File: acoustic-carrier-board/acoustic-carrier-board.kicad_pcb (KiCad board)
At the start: 6 copper layers, 99 x 97 mm, 445 parts, among them IC1 ECP5-BGA256, IC1101 MT41K256M16TW-107_P, J1001 BWU.FL-IPEX1, J1002 BWU.FL-IPEX1, J1003 BWU.FL-IPEX1, J1004 BWU.FL-IPEX1, J1005 BWU.FL-IPEX1, J1006 BWU.FL-IPEX1, J1007 8P8C_Shielded, J1008 BWU.FL-IPEX1, J1009 BWU.FL-IPEX1, J1010 BWU.FL-IPEX1, J1011 BWU.FL-IPEX1, J1201 HR911130A, J201 Conn_02x06_Odd_Even, J701 Conn_02x03_Odd_Even, J702 PMOD_JTAG, J703 PMOD_SPI, J704 PMOD_GPIO, J801 TYPE-C-31-M-12, J903 Conn_02x06_Odd_Even, Q201 AO3401A, SW602 SW_Push, SW603 SW_Push, SW701 SW_Push, U1001 MS9280, U1002 THS4521IDGK, U1003 DGQ2788AEN-T1-GE4, U1004 LMV321, U1005 TL432DBZ, U1201 KSZ9031RN, U201 TPS2121RUX, U202 TLV62569DBV, U203 TLV62569DBV, U204 TLV62569DBV, U205 TLV62569DBV, U206 OPA376xxDBV, U701 W25Q128JVS, U702 W25Q128JVS, U801 USB3300-EZK, U802 LMV321, Y1201 25MHz, Y401 Crystal Oscillator, Y801 Crystal_GND24_Small

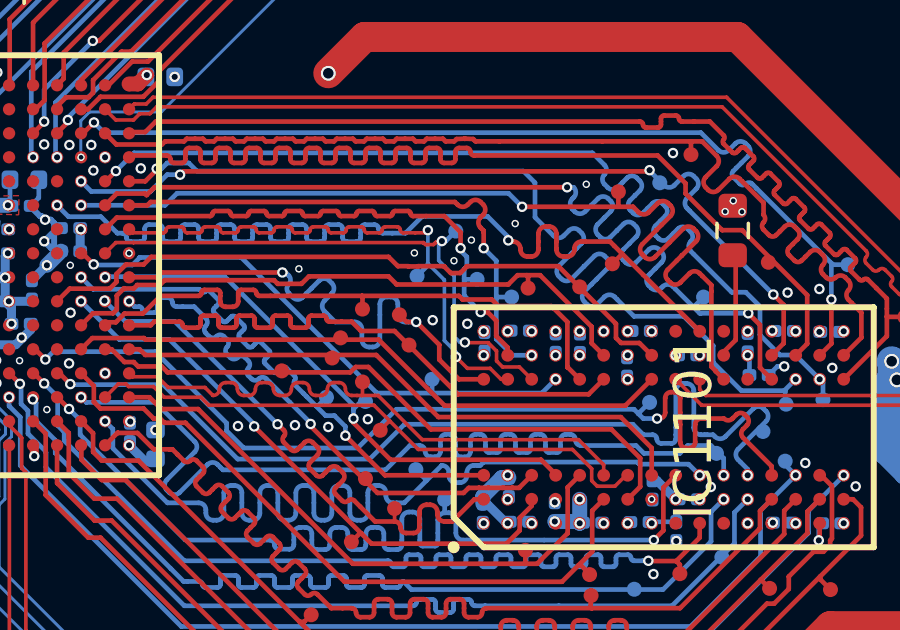
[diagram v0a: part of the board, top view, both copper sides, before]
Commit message: Modified README, lpddr3 testpoint search
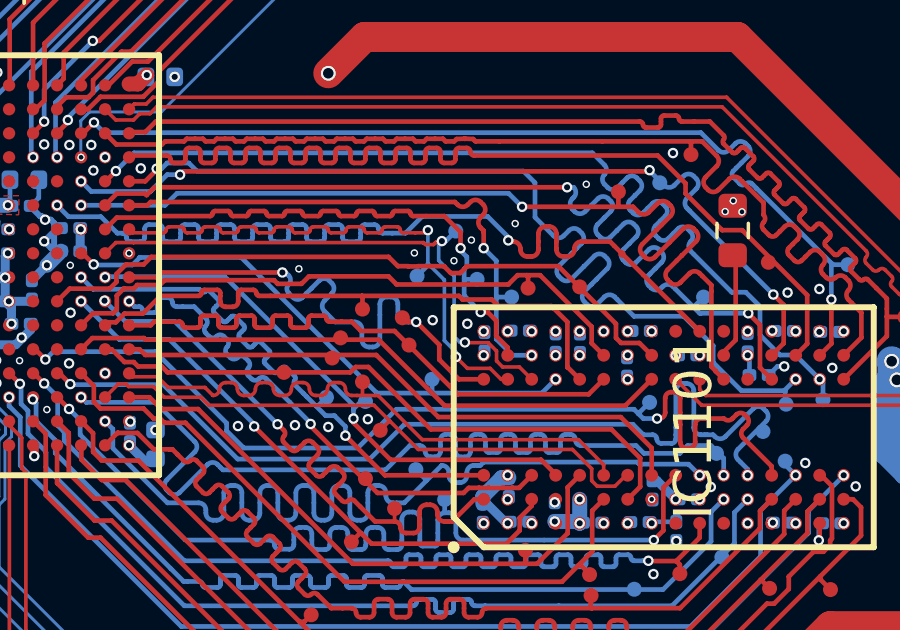
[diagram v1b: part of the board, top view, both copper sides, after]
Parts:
- TP1149: footprint iw-misc:TestPoint_Pad_D0.25mm -> iw-misc:TestPoint_Pad_D0.125mm
- moved TP1149 0.46 mm to (111.3, 87.5)
- moved TP1110 0.14 mm to (104.0, 89.6)
- moved TP1120 0.09 mm to (100.1, 91.4)
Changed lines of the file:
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@@
 	(footprint "iw-misc:TestPoint_Pad_D0.25mm"
 		(layer "F.Cu")
-		(at 103.91 89.5)
+		(at 104.01 89.6)
 		(descr "SMD pad as test Point, diameter 1.0mm")
 		(tags "test point SMD pad")
@@
 		)
 	)
-	(footprint "iw-misc:TestPoint_Pad_D0.25mm"
+	(footprint "iw-misc:TestPoint_Pad_D0.125mm"
 		(layer "F.Cu")
-		(at 111.01 87.8 90)
+		(at 111.33 87.47 90)
 		(descr "SMD pad as test Point, diameter 1.0mm")
 		(tags "test point SMD pad")
@@
 		(fp_circle
 			(center 0 0)
-			(end 0.25 0)
+			(end 0.125 0)
 			(stroke
 				(width 0.05)
@@
 		(pad "1" smd circle
 			(at 0 0 90)
-			(size 0.5 0.5)
+			(size 0.25 0.25)
 			(layers "F.Cu" "F.Mask")
 			(net 130 "/DDR3/DDR3.CKE")
@@
 	(footprint "iw-misc:TestPoint_Pad_D0.25mm"
 		(layer "F.Cu")
-		(at 99.99 91.37 90)
+		(at 100.06 91.42 90)
 		(descr "SMD pad as test Point, diameter 1.0mm")
 		(tags "test point SMD pad")
@@
 	)
 	(segment
-		(start 111.01 87.8)
-		(end 111.33 87.48)
-		(width 0.1565)
-		(layer "F.Cu")
-		(net 130)
-	)
-	(segment
 		(start 108.544067 87.06)
 		(end 108.544067 86.8)
@@
 		(width 0.1565)
 		(layer "F.Cu")
-		(net 130)
-	)
-	(segment
-		(start 111.33 87.48)
-		(end 111.33 87.46)
-		(width 0.1565)
-		(layer "F.Cu")
